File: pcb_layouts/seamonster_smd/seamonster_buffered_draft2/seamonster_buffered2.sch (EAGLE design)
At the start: 132 parts, among them IC1 7808DT, IC2 4051D, IC3 4051D, IC4 DG408DY, IC5 4046D, IC6 40106D, IC7 4070D, IC8 4046D, IC9 4040D, Q1 THONKICONNNEW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

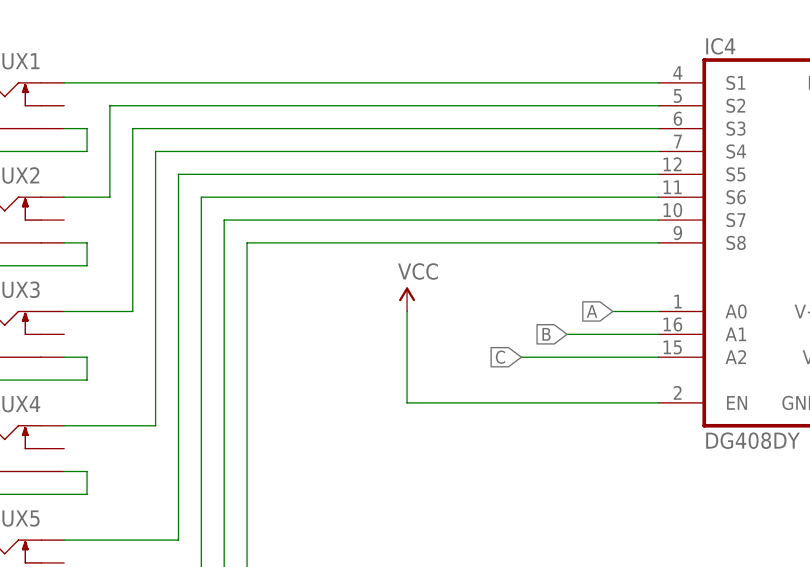
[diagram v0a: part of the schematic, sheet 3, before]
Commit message: finished routing IO to DG408 MUX
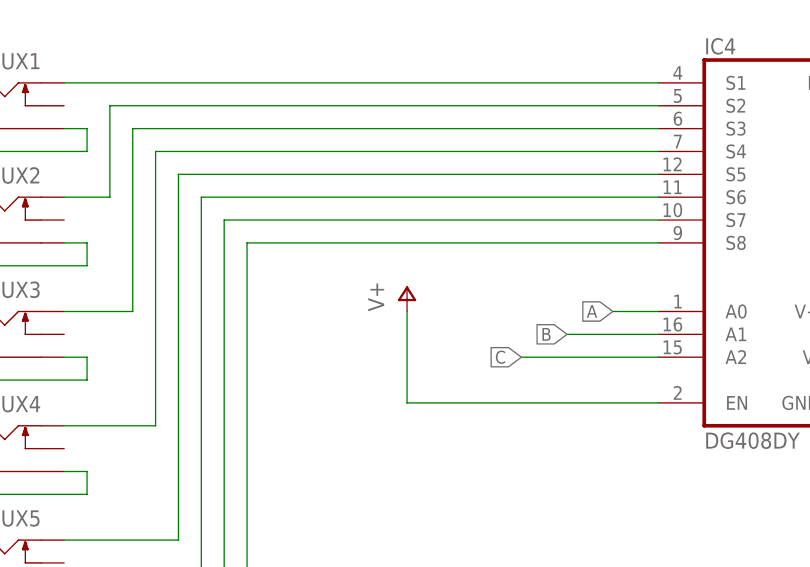
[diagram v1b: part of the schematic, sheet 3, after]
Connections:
- net V+: now also IC4.EN
- net VCC: no longer IC4.EN
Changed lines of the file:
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@@
 <part name="GND48" library="supply1" library_urn="urn:adsk.eagle:library:371" deviceset="GND" device=""/>
 <part name="GND49" library="supply1" library_urn="urn:adsk.eagle:library:371" deviceset="GND" device=""/>
-<part name="SUPPLY17" library="SparkFun-Aesthetics" deviceset="VCC" device=""/>
 <part name="VR15" library="MusicThingModular" deviceset="9MM_SNAP-IN_POT_CHASSIS" device="" value="100KΩ"/>
 <part name="GND50" library="supply1" library_urn="urn:adsk.eagle:library:371" deviceset="GND" device=""/>
@@
 <part name="C35" library="SparkFun-Capacitors" deviceset="CAP" device="0805"/>
 <part name="GND74" library="supply1" library_urn="urn:adsk.eagle:library:371" deviceset="GND" device=""/>
+<part name="P+8" library="supply1" library_urn="urn:adsk.eagle:library:371" deviceset="V+" device=""/>
 </parts>
 <sheets>
@@
 <instance part="GND48" gate="1" x="360.68" y="58.42"/>
 <instance part="GND49" gate="1" x="370.84" y="66.04"/>
-<instance part="SUPPLY17" gate="G$1" x="284.48" y="91.44"/>
 <instance part="GND73" gate="1" x="251.46" y="218.44"/>
 <instance part="J1" gate="G$1" x="132.08" y="68.58"/>
 <instance part="J2" gate="G$1" x="132.08" y="55.88"/>
 <instance part="J3" gate="G$1" x="132.08" y="43.18"/>
+<instance part="P+8" gate="1" x="284.48" y="93.98"/>
 </instances>
 <busses>
@@
 <junction x="353.06" y="91.44"/>
 </segment>
+<segment>
+<wire x1="284.48" y1="91.44" x2="284.48" y2="81.28" width="0.1524" layer="91"/>
+<pinref part="IC4" gate="G$2" pin="EN"/>
+<wire x1="284.48" y1="81.28" x2="312.42" y2="81.28" width="0.1524" layer="91"/>
+<pinref part="P+8" gate="1" pin="V+"/>
+</segment>
 </net>
 <net name="V-" class="0">
@@
 <pinref part="VR8" gate="G$1" pin="E"/>
 </segment>
-<segment>
-<pinref part="SUPPLY17" gate="G$1" pin="VCC"/>
-<wire x1="284.48" y1="91.44" x2="284.48" y2="81.28" width="0.1524" layer="91"/>
-<pinref part="IC4" gate="G$2" pin="EN"/>
-<wire x1="284.48" y1="81.28" x2="312.42" y2="81.28" width="0.1524" layer="91"/>
-</segment>
-</net>
+</net>

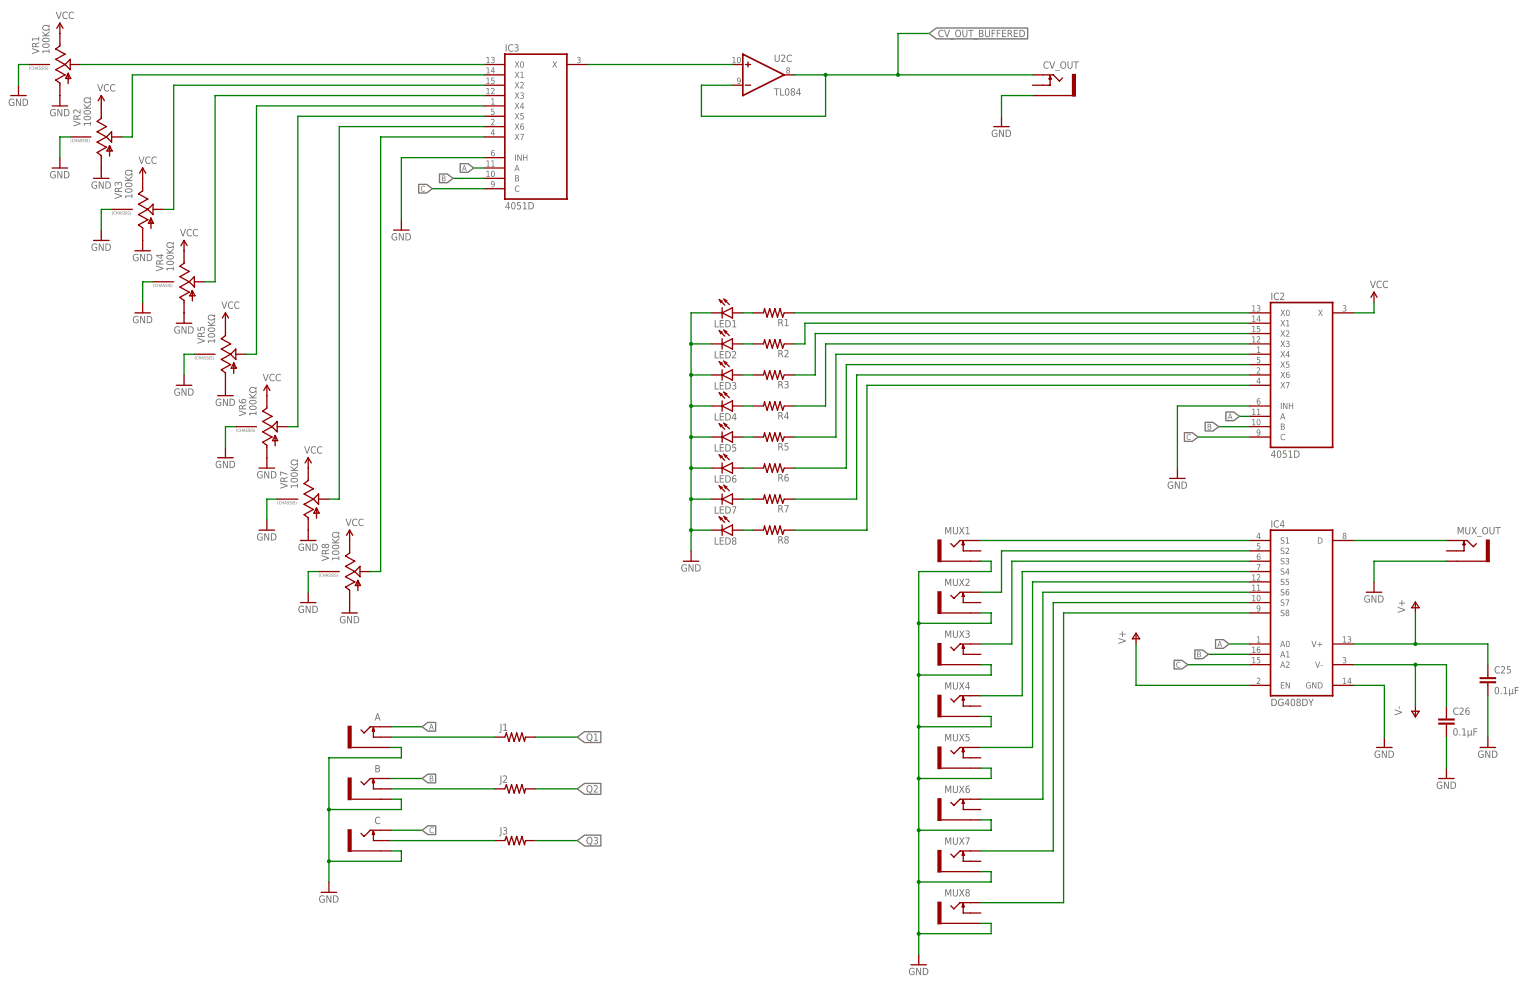
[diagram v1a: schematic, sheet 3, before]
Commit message: added to-do text file for PCB revisions
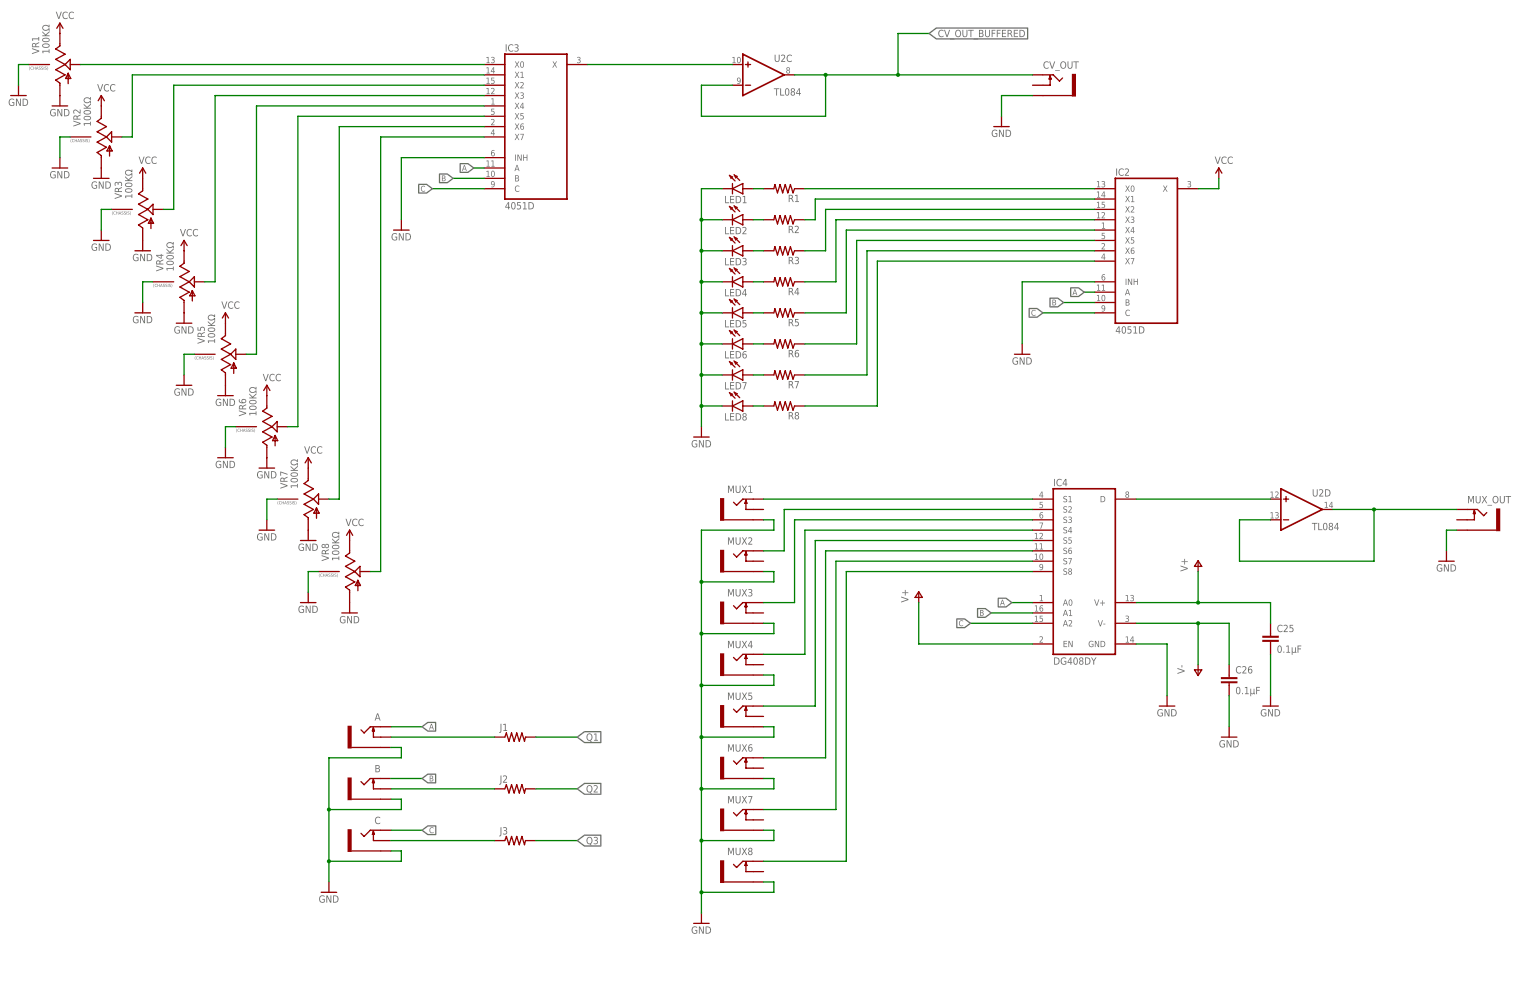
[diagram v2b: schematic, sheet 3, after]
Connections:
- new net N$9: MUX_OUT.TIP, U2D.-IN, U2D.OUT
- net N$1: now also U2D.+IN; no longer MUX_OUT.TIP
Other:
- moved on the sheet: C25, C26, IC2, IC4, LED1, LED2, LED3, LED4, LED5, LED6, LED7, LED8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
